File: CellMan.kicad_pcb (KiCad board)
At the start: 2 copper layers, 99.4 x 45 mm, 72 parts, among them J1 Conn_01x04_Male, J2 Conn_01x04_Male, J3 Conn_01x04_Male, J4 Conn_01x02_Female, J5 Conn_01x03_Male, Q1 BSS138W, Q2 STS8DN6LF6AG, Q4 BSS138W, Q5 BSS138W, SW1 SW_DIP_x06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

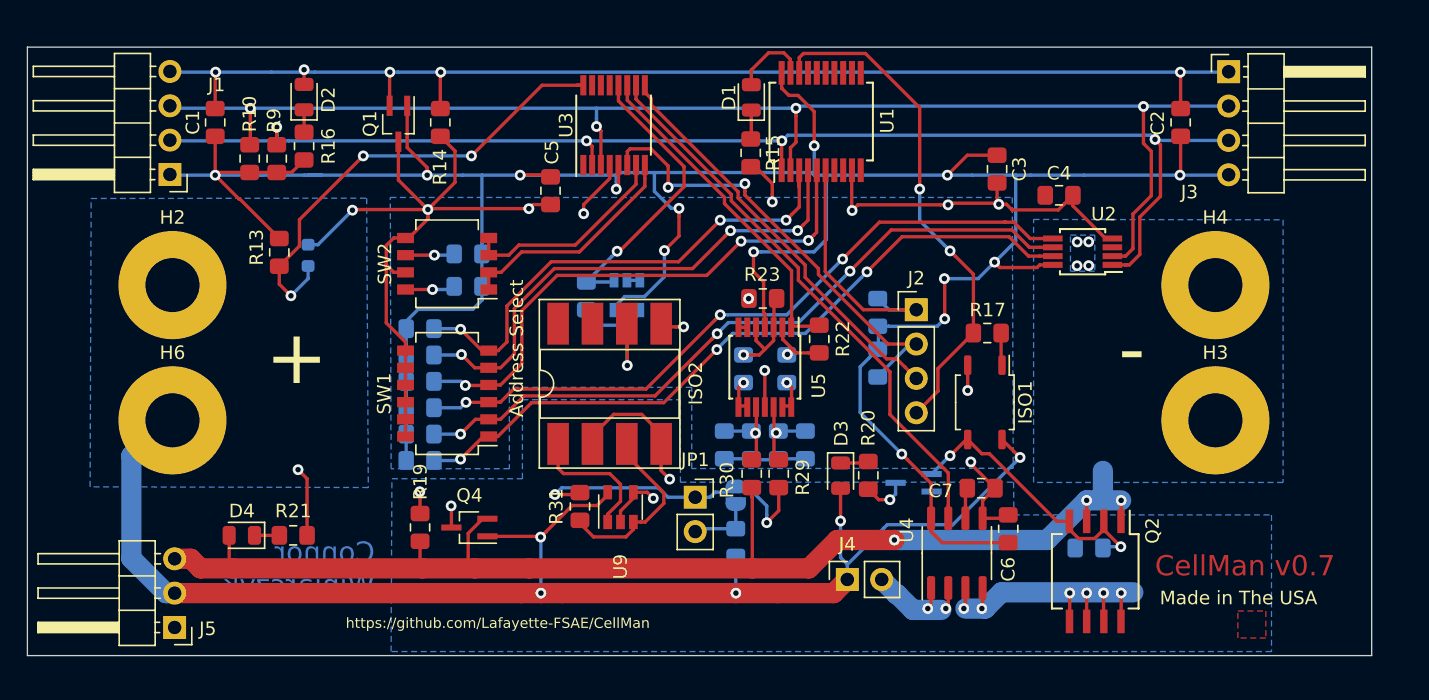
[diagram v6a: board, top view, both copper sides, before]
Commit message: added solder mask for serial number
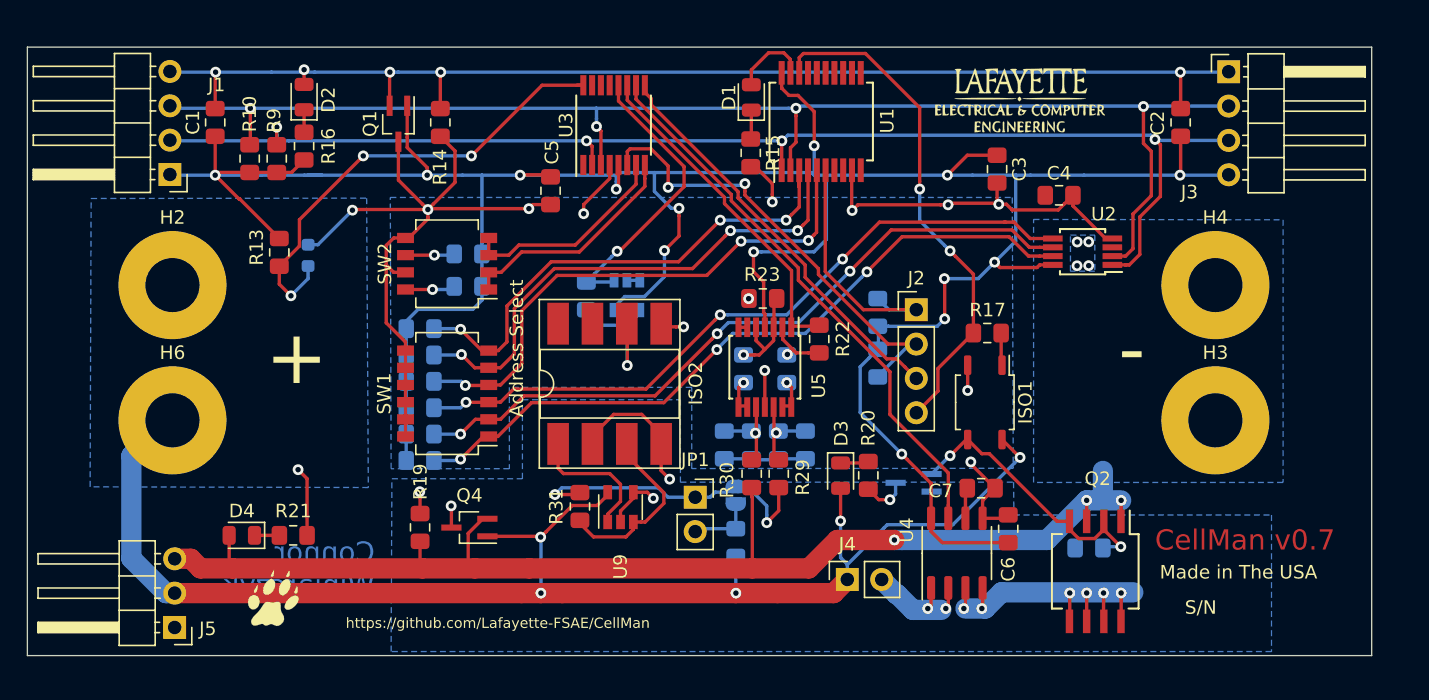
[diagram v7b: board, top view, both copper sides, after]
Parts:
- added G***: LOGO, Lafayette_Electric_Car_Footprints:Paw, F.Cu at (109.9, 123.2)
- added G***: LOGO, Lafayette_Electric_Car_Footprints:ECE_Logo, F.Cu at (165.1, 86.4)
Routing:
- removed copper zone on F.Cu, net (none)
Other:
- board text added: "S/N"

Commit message: made dimensions even
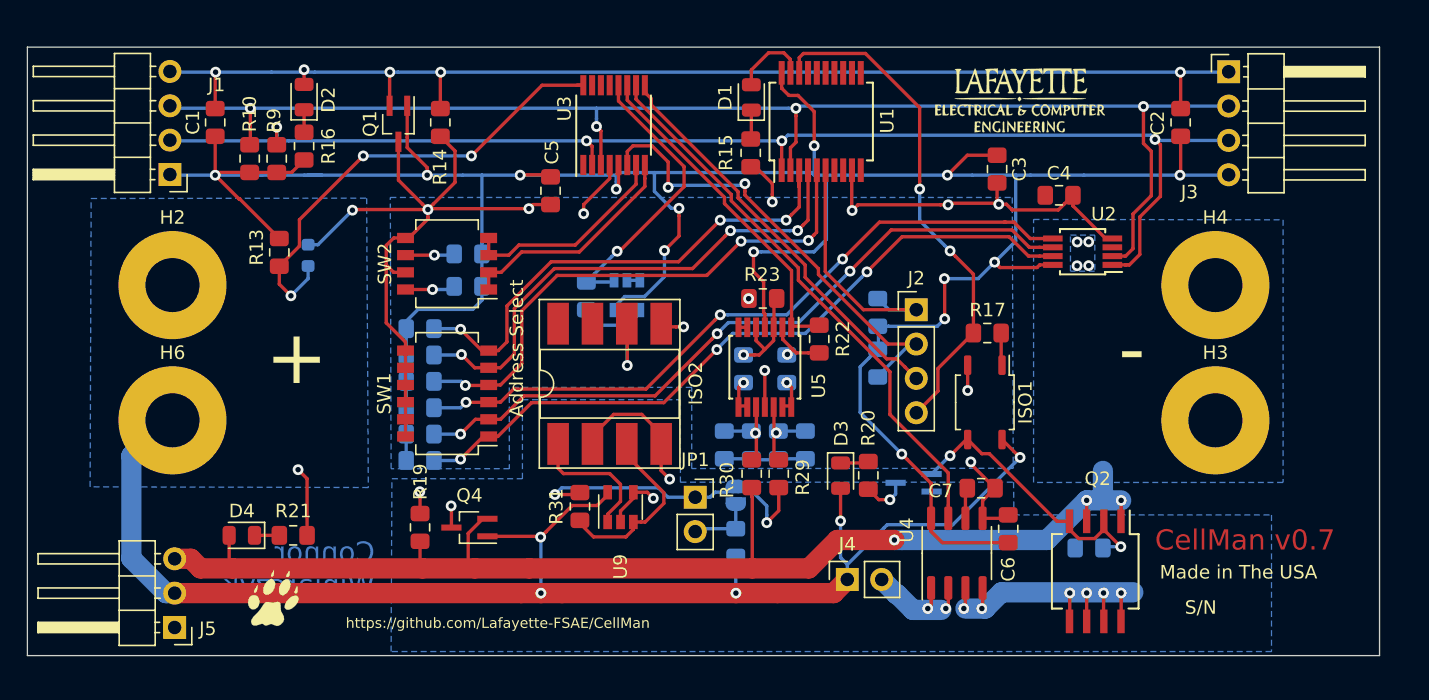
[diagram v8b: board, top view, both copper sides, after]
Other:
- board size 99.4 x 45 mm -> 100 x 45 mm
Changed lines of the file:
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@@
     (tags "SSOP 0.65")
     (attr smd)
-    (fp_text reference U3 (at 0 -3.55 90) (layer F.SilkS)
+    (fp_text reference U3 (at 1.22 -3.67 90) (layer F.SilkS)
       (effects (font (size 1 1) (thickness 0.15)))
     )
@@
     (tags diode)
     (attr smd)
-    (fp_text reference D1 (at 0 -1.65 90) (layer F.SilkS)
+    (fp_text reference D1 (at 0 -1.93 90) (layer F.SilkS)
       (effects (font (size 1 1) (thickness 0.15)))
     )
@@
     (tags "resistor handsolder")
     (attr smd)
-    (fp_text reference R15 (at 0 -1.65 270) (layer F.SilkS)
+    (fp_text reference R15 (at -0.02 1.835 270) (layer F.SilkS)
       (effects (font (size 1 1) (thickness 0.15)))
     )
@@
     )
   )
+  (dimension 45 (width 0.12) (layer Dwgs.User)
+    (gr_text "45 mm" (at 195.11 104.88 270) (layer Dwgs.User)
+      (effects (font (size 1 1) (thickness 0.15)))
+    )
+    (feature1 (pts (xy 191.66 127.38) (xy 194.426421 127.38)))
+    (feature2 (pts (xy 191.66 82.38) (xy 194.426421 82.38)))
+    (crossbar (pts (xy 193.84 82.38) (xy 193.84 127.38)))
+    (arrow1a (pts (xy 193.84 127.38) (xy 193.253579 126.253496)))
+    (arrow1b (pts (xy 193.84 127.38) (xy 194.426421 126.253496)))
+    (arrow2a (pts (xy 193.84 82.38) (xy 193.253579 83.506504)))
+    (arrow2b (pts (xy 193.84 82.38) (xy 194.426421 83.506504)))
+  )
+  (dimension 100 (width 0.12) (layer Dwgs.User)
+    (gr_text "100 mm" (at 141.66 78.68) (layer Dwgs.User)
+      (effects (font (size 1 1) (thickness 0.15)))
+    )
+    (feature1 (pts (xy 191.66 82.38) (xy 191.66 79.363579)))
+    (feature2 (pts (xy 91.66 82.38) (xy 91.66 79.363579)))
+    (crossbar (pts (xy 91.66 79.95) (xy 191.66 79.95)))
+    (arrow1a (pts (xy 191.66 79.95) (xy 190.533496 80.536421)))
+    (arrow1b (pts (xy 191.66 79.95) (xy 190.533496 79.363579)))
+    (arrow2a (pts (xy 91.66 79.95) (xy 92.786504 80.536421)))
+    (arrow2b (pts (xy 91.66 79.95) (xy 92.786504 79.363579)))
+  )
   (gr_text S/N (at 178.435 123.825) (layer F.SilkS)
     (effects (font (size 1 1) (thickness 0.15)))
@@
     (effects (font (size 0.762 0.762) (thickness 0.1905)))
   )
-  (dimension 44.98001 (width 0.15) (layer Dwgs.User)
-    (gr_text "1.7709 in" (at 198.364052 104.885132 270.0382142) (layer Dwgs.User)
-      (effects (font (size 1 1) (thickness 0.15)))
-    )
-    (feature1 (pts (xy 191.08 127.38) (xy 197.665472 127.375608)))
-    (feature2 (pts (xy 191.05 82.4) (xy 197.635472 82.395608)))
-    (crossbar (pts (xy 197.049052 82.395999) (xy 197.079052 127.375999)))
-    (arrow1a (pts (xy 197.079052 127.375999) (xy 196.49188 126.249887)))
-    (arrow1b (pts (xy 197.079052 127.375999) (xy 197.664721 126.249104)))
-    (arrow2a (pts (xy 197.049052 82.395999) (xy 196.463383 83.522894)))
-    (arrow2b (pts (xy 197.049052 82.395999) (xy 197.636224 83.522111)))
-  )
-  (dimension 99.390002 (width 0.12) (layer Dwgs.User)
-    (gr_text "3.9130 in" (at 141.356255 76.154237) (layer Dwgs.User)
-      (effects (font (size 1 1) (thickness 0.15)))
-    )
-    (feature1 (pts (xy 191.05 82.4) (xy 191.051117 76.847816)))
-    (feature2 (pts (xy 91.66 82.38) (xy 91.661117 76.827816)))
-    (crossbar (pts (xy 91.660999 77.414237) (xy 191.050999 77.434237)))
-    (arrow1a (pts (xy 191.050999 77.434237) (xy 189.924377 78.020431)))
-    (arrow1b (pts (xy 191.050999 77.434237) (xy 189.924613 76.84759)))
-    (arrow2a (pts (xy 91.660999 77.414237) (xy 92.787385 78.000884)))
-    (arrow2b (pts (xy 91.660999 77.414237) (xy 92.787621 76.828043)))
-  )
   (gr_text "Made in The USA\n" (at 175.4 121.215) (layer F.SilkS)
     (effects (font (size 1 1) (thickness 0.15)) (justify left))
@@
     (effects (font (size 1.5 1.5) (thickness 0.3)) (justify left mirror))
   )
-  (gr_line (start 191.08 82.38) (end 191.08 127.38) (layer Edge.Cuts) (width 0.05))
-  (gr_line (start 91.66 82.38) (end 191.08 82.38) (layer Edge.Cuts) (width 0.05))
-  (gr_line (start 91.66 127.38) (end 191.08 127.38) (layer Edge.Cuts) (width 0.05))
+  (gr_line (start 191.66 82.38) (end 191.66 127.38) (layer Edge.Cuts) (width 0.05))
+  (gr_line (start 91.66 82.38) (end 191.66 82.38) (layer Edge.Cuts) (width 0.05))
+  (gr_line (start 91.66 127.38) (end 191.66 127.38) (layer Edge.Cuts) (width 0.05))
   (gr_line (start 91.66 82.38) (end 91.66 127.38) (layer Edge.Cuts) (width 0.05))
   (segment (start 109.72 84.23) (end 112.07 84.23) (width 0.25) (layer B.Cu) (net 1))
@@
   (via (at 139.050002 92.75) (size 0.8) (drill 0.4) (layers F.Cu B.Cu) (net 19))
   (segment (start 139.050002 92.975) (end 139.050002 93.000002) (width 0.25) (layer B.Cu) (net 19))
-  (segment (start 139.050002 92.409315) (end 139.050002 92.975) (width 0.25) (layer F.Cu) (net 19))
-  (segment (start 139.050002 91.1678) (end 139.050002 92.409315) (width 0.25) (layer F.Cu) (net 19))
-  (segment (start 137.782202 89.9) (end 139.050002 91.1678) (width 0.25) (layer F.Cu) (net 19))
-  (segment (start 136.225 89.9) (end 137.782202 89.9) (width 0.25) (layer F.Cu) (net 19))
-  (segment (start 136.025 90.1) (end 136.225 89.9) (width 0.25) (layer F.Cu) (net 19))
-  (segment (start 136.025 91.1) (end 136.025 90.1) (width 0.25) (layer F.Cu) (net 19))
   (via (at 144.726122 92.473878) (size 0.8) (drill 0.4) (layers F.Cu B.Cu) (net 19))
   (segment (start 144.6 92.6) (end 144.726122 92.473878) (width 0.25) (layer B.Cu) (net 19))
@@
   (segment (start 144.726122 93.039563) (end 144.726122 92.473878) (width 0.25) (layer F.Cu) (net 19))
   (segment (start 150.162977 99.191457) (end 150.162977 98.762978) (width 0.25) (layer F.Cu) (net 19))
+  (segment (start 139.050002 92.409315) (end 139.050002 92.975) (width 0.25) (layer F.Cu) (net 19))
+  (segment (start 139.050002 90.870002) (end 139.050002 92.409315) (width 0.25) (layer F.Cu) (net 19))
+  (segment (start 137.86 89.68) (end 139.050002 90.870002) (width 0.25) (layer F.Cu) (net 19))
+  (segment (start 136.445 89.68) (end 137.86 89.68) (width 0.25) (layer F.Cu) (net 19))
+  (segment (start 136.025 91.1) (end 136.025 90.1) (width 0.25) (layer F.Cu) (net 19))
+  (segment (start 136.025 90.1) (end 136.445 89.68) (width 0.25) (layer F.Cu) (net 19))
   (segment (start 155.375 101.8) (end 157.4 101.8) (width 0.25) (layer B.Cu) (net 20))
   (segment (start 154.55 100.975) (end 155.375 101.8) (width 0.25) (layer B.Cu) (net 20))
